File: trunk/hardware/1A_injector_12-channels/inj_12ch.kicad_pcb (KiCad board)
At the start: 2 copper layers, 47 x 58.9 mm, 58 parts, among them P1 CONN_3, P2 CONN_10X2, P3 CONN_16, P4 CONN_1, P5 CONN_1, Q1 OVP_DRIVER, Q10 OVP_DRIVER, Q11 OVP_DRIVER, Q12 OVP_DRIVER, Q2 OVP_DRIVER, Q3 OVP_DRIVER, Q4 OVP_DRIVER, Q5 OVP_DRIVER, Q6 OVP_DRIVER, Q7 OVP_DRIVER, Q8 OVP_DRIVER, Q9 OVP_DRIVER

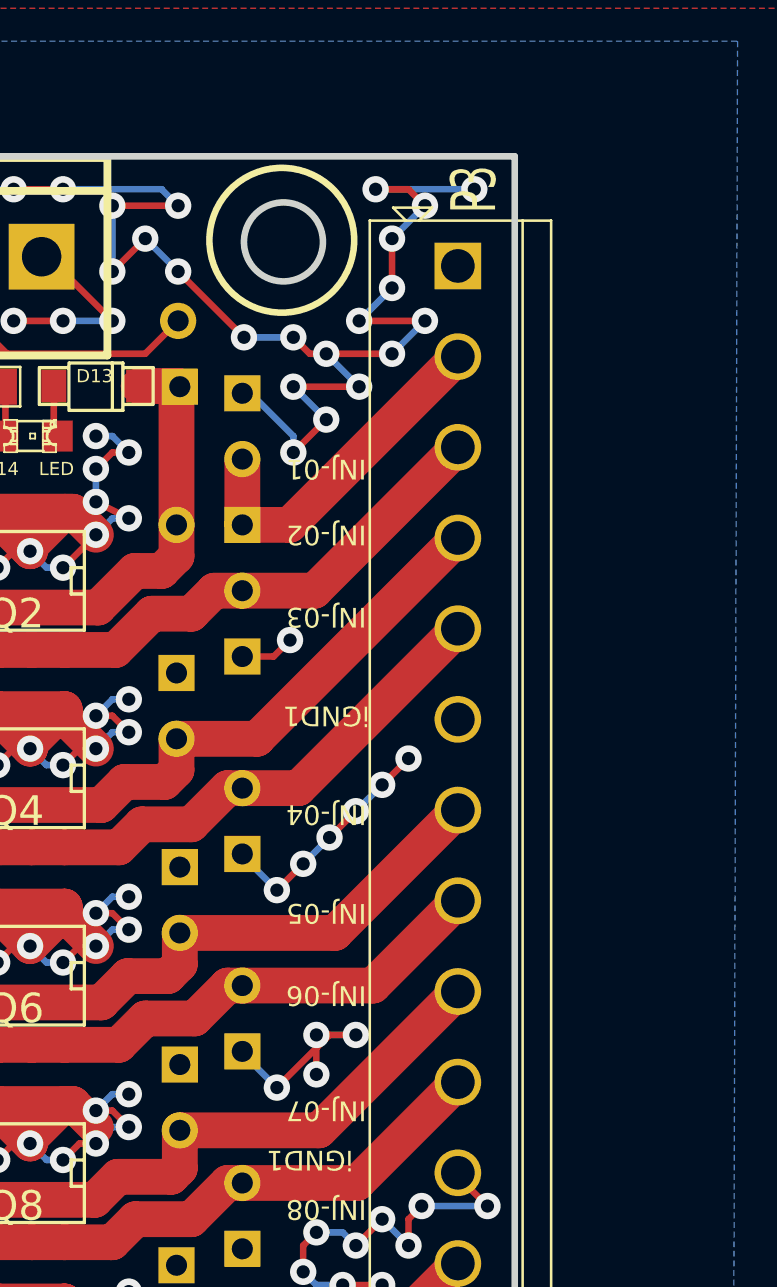
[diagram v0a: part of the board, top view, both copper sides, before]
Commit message: 
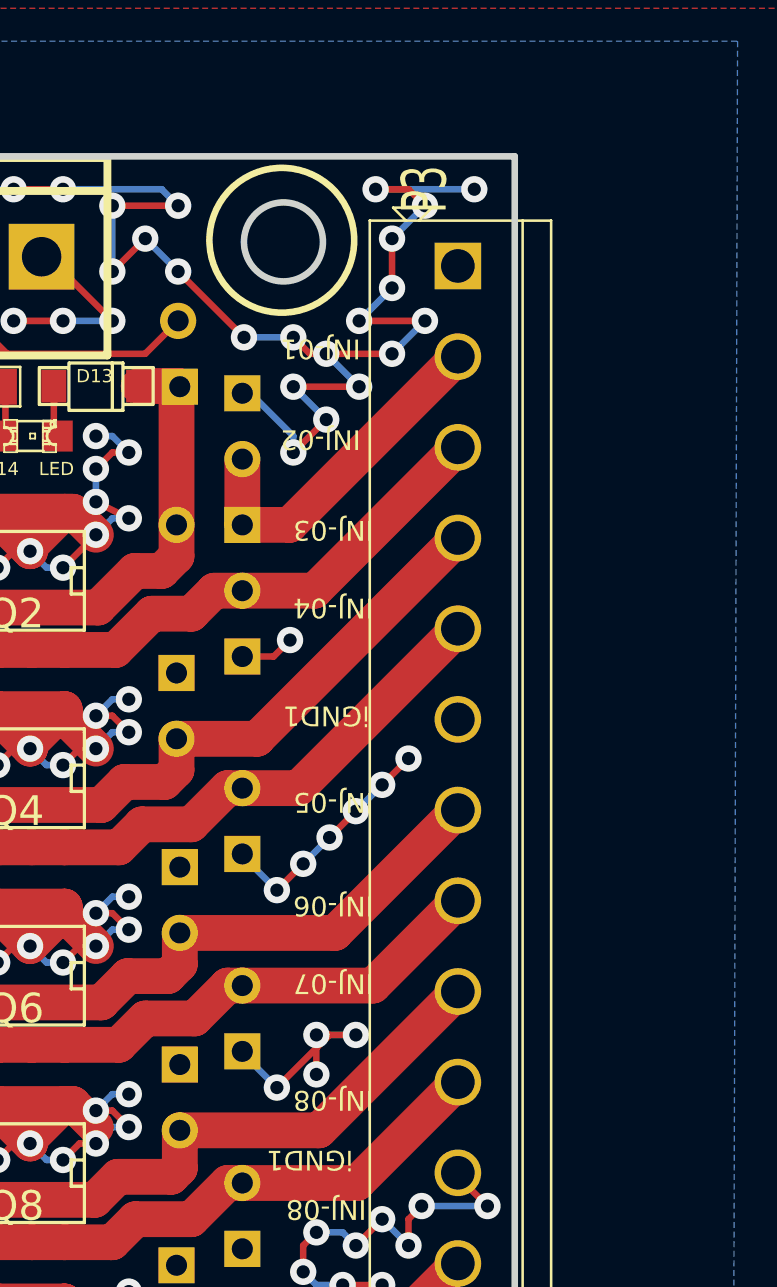
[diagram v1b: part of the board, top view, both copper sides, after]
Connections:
- net /3V renamed /3.3V

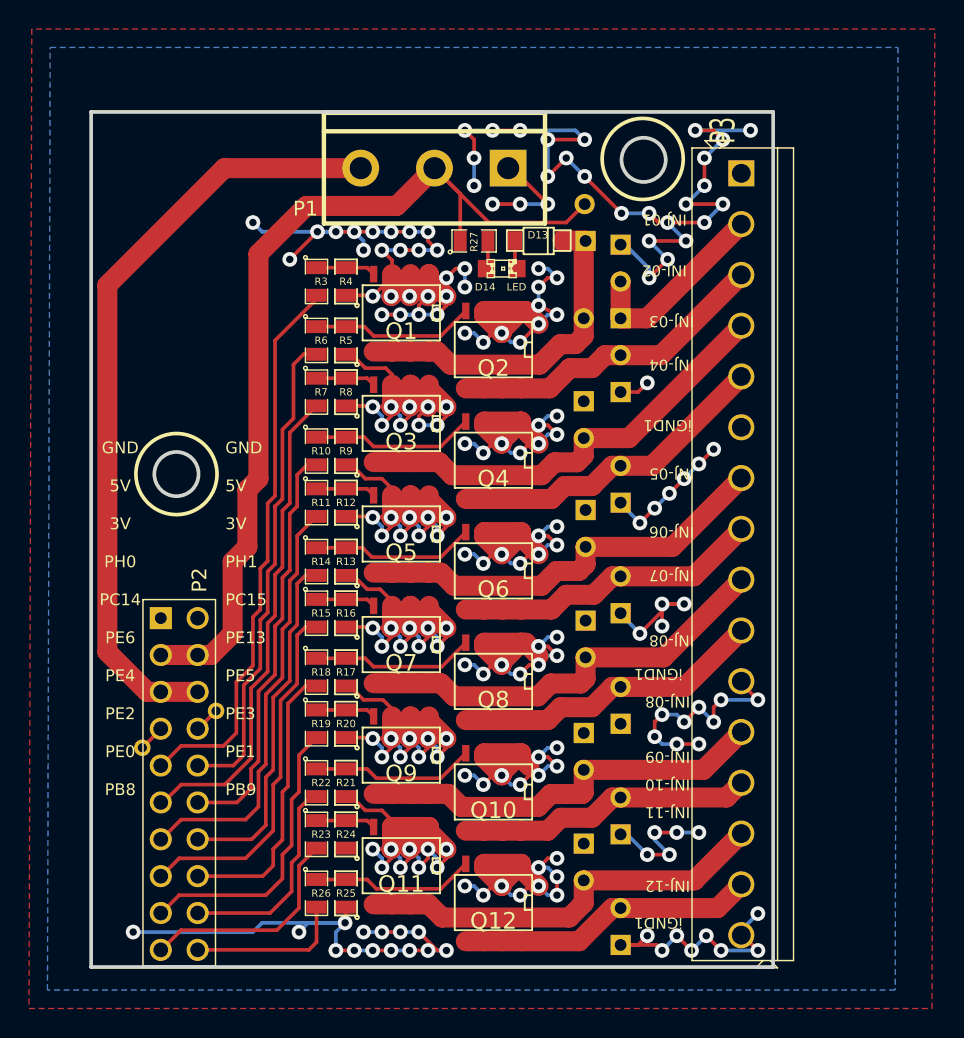
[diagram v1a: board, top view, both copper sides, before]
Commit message: component re-annotation
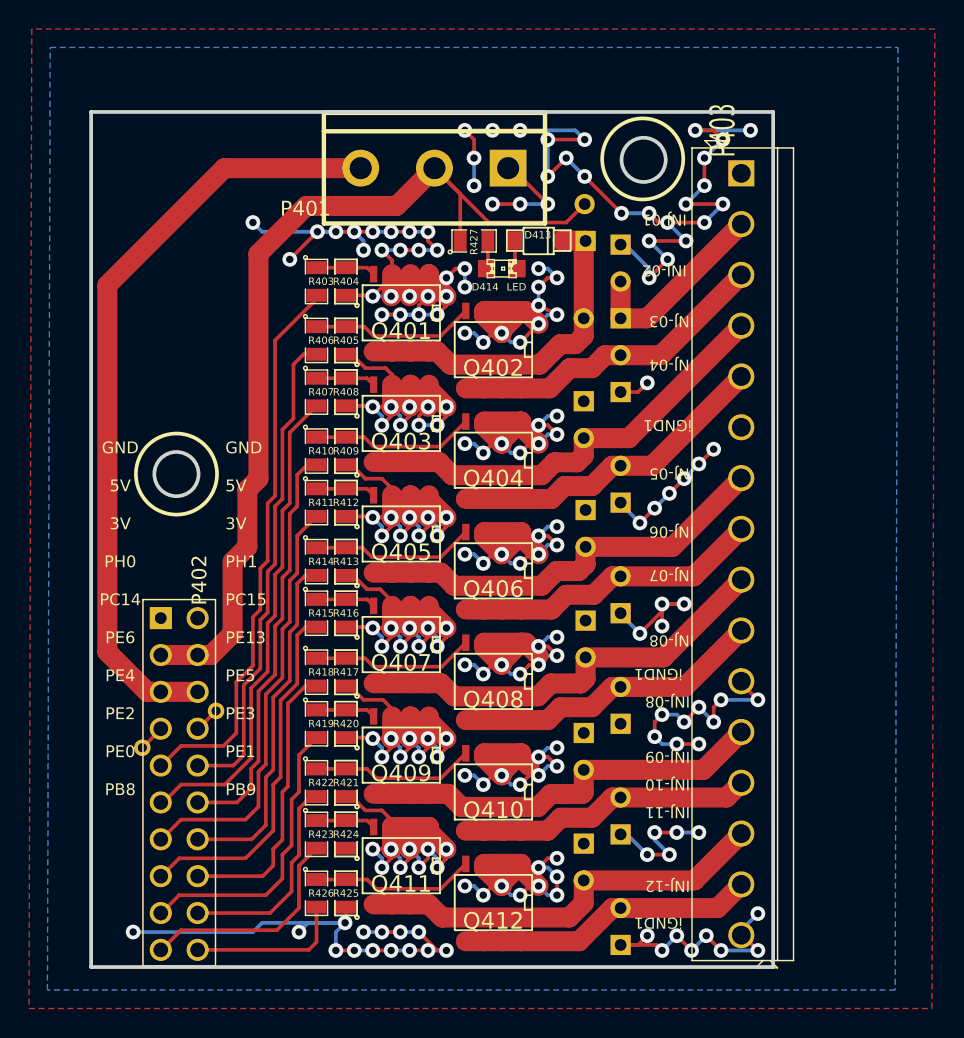
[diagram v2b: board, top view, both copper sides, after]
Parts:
- renumbered D1 to D401, D2 to D402, D3 to D403, D4 to D404, D5 to D405, D6 to D406, D7 to D407, D8 to D408, D9 to D409, D10 to D410, D11 to D411, D12 to D412, D13 to D413, D14 to D414, P1 to P401, P2 to P402, P3 to P403, P4 to P404, P5 to P405, Q1 to Q401, Q2 to Q402, Q3 to Q403, Q4 to Q404, Q5 to Q405, Q6 to Q406, Q7 to Q407, Q8 to Q408, Q9 to Q409, Q10 to Q410, Q11 to Q411, Q12 to Q412, R1 to R401, R2 to R402, R3 to R403, R4 to R404, R5 to R405, R6 to R406, R7 to R407, R8 to R408, R9 to R409, R10 to R410, R11 to R411, R12 to R412, R13 to R413, R14 to R414, R15 to R415, R16 to R416, R17 to R417, R18 to R418, R19 to R419, R20 to R420, R21 to R421, R22 to R422, R23 to R423, R24 to R424, R25 to R425, R26 to R426, R27 to R427

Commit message: 3V track moved
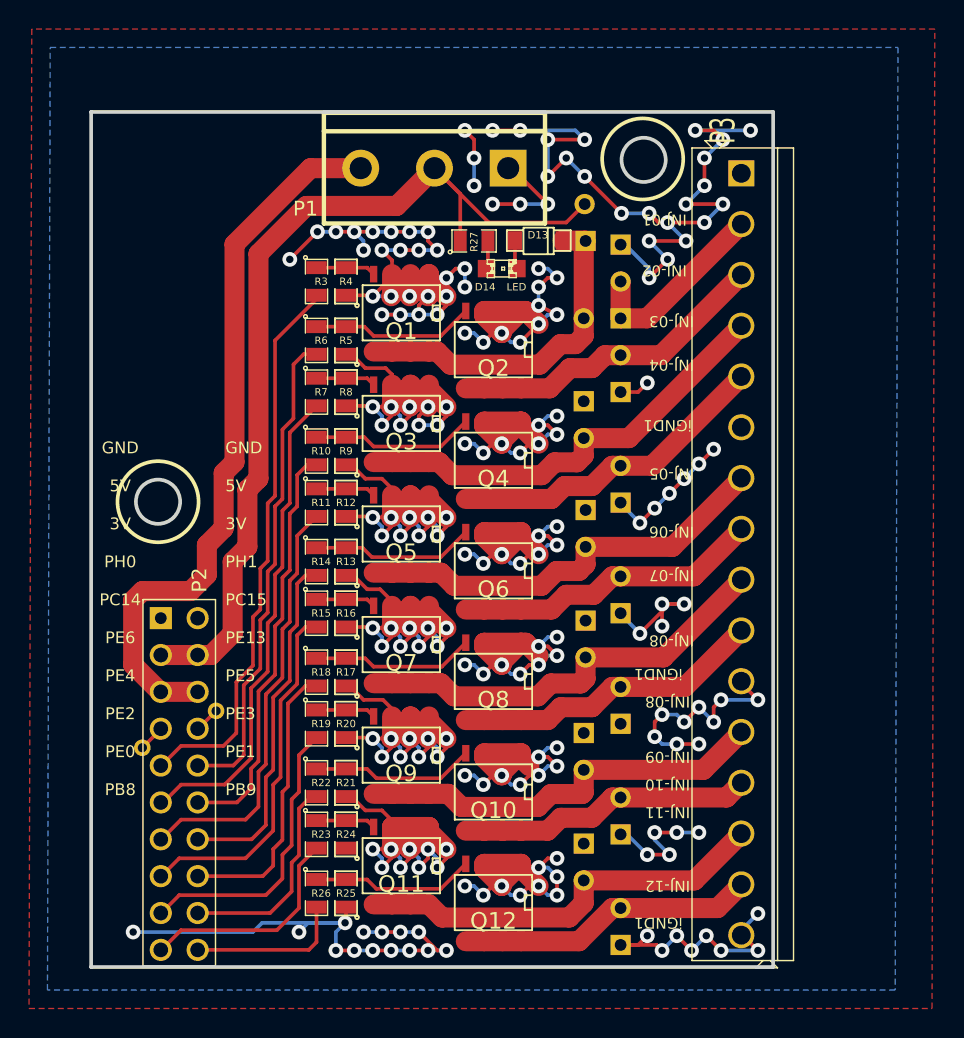
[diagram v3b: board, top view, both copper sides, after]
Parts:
- renumbered D401 to D1, D410 to D10, D411 to D11, D412 to D12, D413 to D13, D414 to D14, D402 to D2, D403 to D3, D404 to D4, D405 to D5, D406 to D6, D407 to D7, D408 to D8, D409 to D9, P401 to P1, P402 to P2, P403 to P3, P404 to P4, P405 to P5, Q401 to Q1, Q410 to Q10, Q411 to Q11, Q412 to Q12, Q402 to Q2, Q403 to Q3, Q404 to Q4, Q405 to Q5, Q406 to Q6, Q407 to Q7, Q408 to Q8, Q409 to Q9, R401 to R1, R410 to R10, R411 to R11, R412 to R12, R413 to R13, R414 to R14, R415 to R15, R416 to R16, R417 to R17, R418 to R18, R419 to R19, R402 to R2, R420 to R20, R421 to R21, R422 to R22, R423 to R23, R424 to R24, R425 to R25, R426 to R26, R427 to R27, R403 to R3, R404 to R4, R405 to R5, R406 to R6, R407 to R7, R408 to R8, R409 to R9
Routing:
- net GND: track 475.5 -> 468.2 mm, vias 197 -> 196
- net /3.3V: track 53.4 -> 49.9 mm
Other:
- outline, holes or cut-outs redrawn
